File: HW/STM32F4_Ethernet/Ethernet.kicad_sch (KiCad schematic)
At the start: 23 parts, among them J1 LU1T516-43, J2 LU1T516-43, U1 KSZ8863MLLI

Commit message: Progress backup
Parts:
- added C? (x4): 100uF, symbol Device:C_Small
- added C? (x6): 100nF, symbol Device:C_Small
- added C?: 10uF, symbol Device:C
- added D?: 1N4148W, Diode_SMD:D_SOD-123, symbol Diode:1N4148W
- added FB? (x2): MPZ1608S601A, BEADC1608X95N, symbol MPZ1608S601A:MPZ1608S601A
- added FB?: FerriteBead, symbol Device:FerriteBead
- added R? (x3): 10K, symbol Device:R_Small
- added R?: 11.8K, symbol Device:R_Small
- added R? (x2): 4.7K, symbol Device:R_Small
- added R?: 10K, symbol Device:R
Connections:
- net GLED_1 is gone; now on net P1LED0: R1.2
- net GLED_2 is gone; now on net P2LED0: R7.2
- net RLED_1 is gone; now on net P1LED1: R2.2
- net RLED_2 is gone; now on net P2LED1: R8.2
- net +3V3: now also U1.22 (VDDIO), U1.40 (VDDIO_2), C?.1, C?.1, C?.1, D?.1 (K), FB?.1, R?.1, R?.1, R?.1, R?.1
- net GND: now also C?.2, C?.2, C?.2, C?.2, C?.2, C?.2, C?.2, C?.2, C?.2, C?.2, C?.2, FB?.2, R?.2, R?.2, R?.2
- net GNDREF: now also FB?.1
- net RXM1: now also U1.1 (RXM1)
- net RXM2: now also U1.8 (RXM2)
- net RXP1: now also U1.2 (RXP1)
- net RXP2: now also U1.9 (RXP2)
- net TXM1: now also U1.3 (TXM1)
- net TXM2: now also U1.11 (TXM2)
- net TXP1: now also U1.4 (TXP1)
- net TXP2: now also U1.12 (TXP2)
- net CLK_25Mhz: now reaches U1.14 (X1)
- net MII_TX_EN: now reaches U1.16 (SMTXEN3)
- net MII_TXD3: now reaches U1.17 (SMTXD33/E_REFCLK_3)
- net MII_TXD2: now reaches U1.18 (SMTXD32)
- net MII_TXD1: now reaches U1.19 (SMTDX31)
- net MII_TXD0: now reaches U1.20 (SMTXD30)
- net MII_TX_CLK: now reaches U1.23 (SMTXC3/REFCLK_3)
- net MII_LINK_MODE: now reaches U1.24 (SMTXER3/MII_LINK_3)
- net MII_LINK_MODE: now also R?.1
- net MII_RX_DV: now reaches U1.25 (SMRXDV3)
- net MII_RXD3: now reaches U1.26 (SMRXD33/REFCLKO_3)
- net MII_RXD2: now reaches U1.27 (SMRXD32)
- net MII_RXD1: now reaches U1.28 (SMRXD31)
- net MII_RXD0: now reaches U1.29 (SMRXD30)
- net MII_RX_CLK: now reaches U1.30 (SMRXC3)
- net +1V8: now reaches U1.32 (VDDC)
- net +1V8: now also U1.42 (VDDC0), C?.1, C?.1, C?.1, FB?.1
- net MII_COL: now reaches U1.33 (SCOL3)
- net MII_CRS: now reaches U1.34 (SCRS3)
- net ~{MII_INTRN}: now reaches U1.35 (INTRN)
- net PHY_SPI_CLK: now reaches U1.36 (SCL_MDC)
- net PHY_SPI_MOSI: now reaches U1.37 (SDA_MDIO)
- net PHY_SPI_MISO: now reaches U1.38 (SPIQ)
- net PHY_SPI_CS: now reaches U1.39 (SPISN)
- net P1LED1: now reaches U1.43 (P1LED1)
- net P1LED1: now also R?.2
- net P1LED0: now reaches U1.44 (P1LED0)
- net P1LED0: now also R?.2
- net P2LED1: now reaches U1.45 (P2LED1)
- net P2LED1: now also R?.2
- net P2LED0: now reaches U1.46 (P2LED0)
- net P2LED0: now also R?.1
- net ~{PHY_RESET}: now reaches U1.47 (RSTN)
- net ~{PHY_RESET}: now also C?.1, D?.2 (A), R?.2
- net PHY_3V3A: now reaches U1.5 (VDDA_3.3)
- net PHY_3V3A: now also C?.1, C?.1, FB?.2
- net ISET: now reaches U1.6 (ISET)
- net ISET: now also R?.1
- net ETH_1V8 renamed PHY_1V8A
- net PHY_1V8A: now also C?.1, C?.1, FB?.2
- no-connect marks 6 -> 8
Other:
- note added: "1V8 Pin(32,42)"
- note added: "1V8A Pin(7)"
- note added: "2kV / 1000pF Cap. Included"
- note added: "3V3 Pin(22, 40)"
- note added: "3V3A Pin(5)"
- note added: "LED0 : Green - Link LED1 : Yellow - Speed"
- note added: "MII_TX_CLK: Place L3 Inner Layer"
- note added: "Output Transmit Current w/ 11.8K 1%"
- note added: "P1LED0 Strap option: Enable auto-negotiation on port 1 (P1ANEN) PU = Enable (better to pull up in design) PD = Disable (default)"
- note added: "P1LED1 Strap option: Force the speed on port 1 (P1SPD) PU = Force port 1 to 100BT if P1ANEN = 0 PD = Force port 1 to 10BT if P1ANEN = 0"
- note added: "P2LED1, P2LED0 [0, 0] : I2C Master P2LED1, P2LED0 [0, 1] : I2C Slave P2LED1, P2LED0 [1, 0] : SPI Slave P2LED1, P2LED0 [1, 1] : SMI"
- note added: "P2LED1/P2LED0 [0,0] : I2C MASTER [0,1] : I2C SLAVE [1,0] : SPI SLAVE [1,1] : SMI/MIIM"
- moved on the sheet: U1

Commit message: Progress backup. add SRAM
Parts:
- gave numbers to parts that had none: 22
- renumbered C4 to C25, C3 to C26, C1 to C27, C2 to C28, C5 to C29, C6 to C30, D1 to D3, D2 to D4, R8 to R10, R3 to R13, R4 to R14, R5 to R15, R6 to R16, R9 to R17, R10 to R18, R11 to R19, R12 to R20, R1 to R7, R2 to R8, R7 to R9, U1 to U3

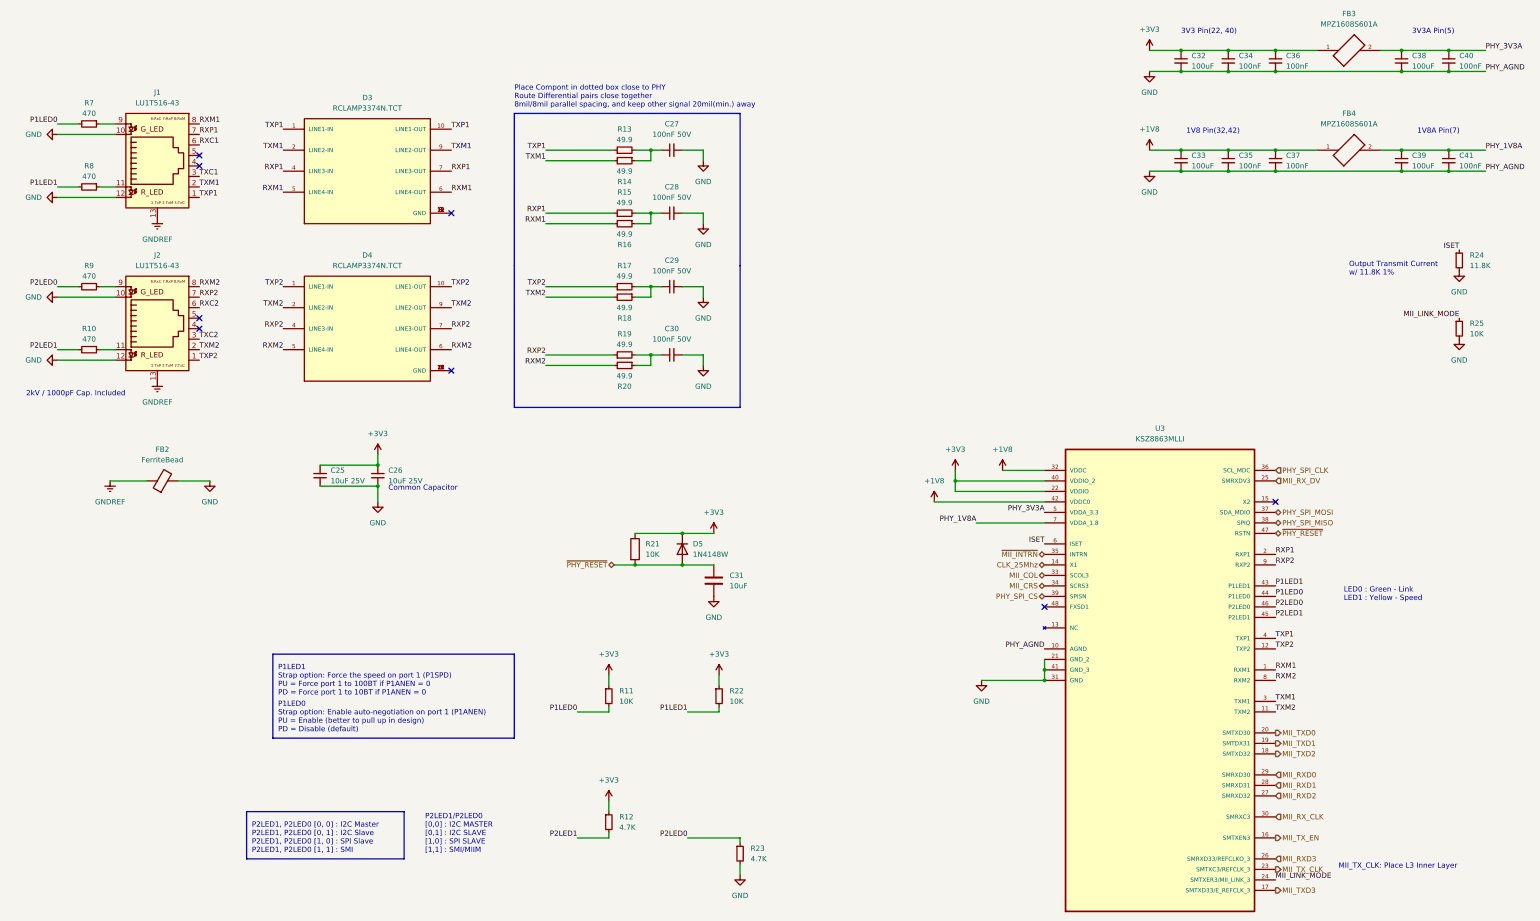
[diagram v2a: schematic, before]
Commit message: Sample PCB. Need to update RLC Size
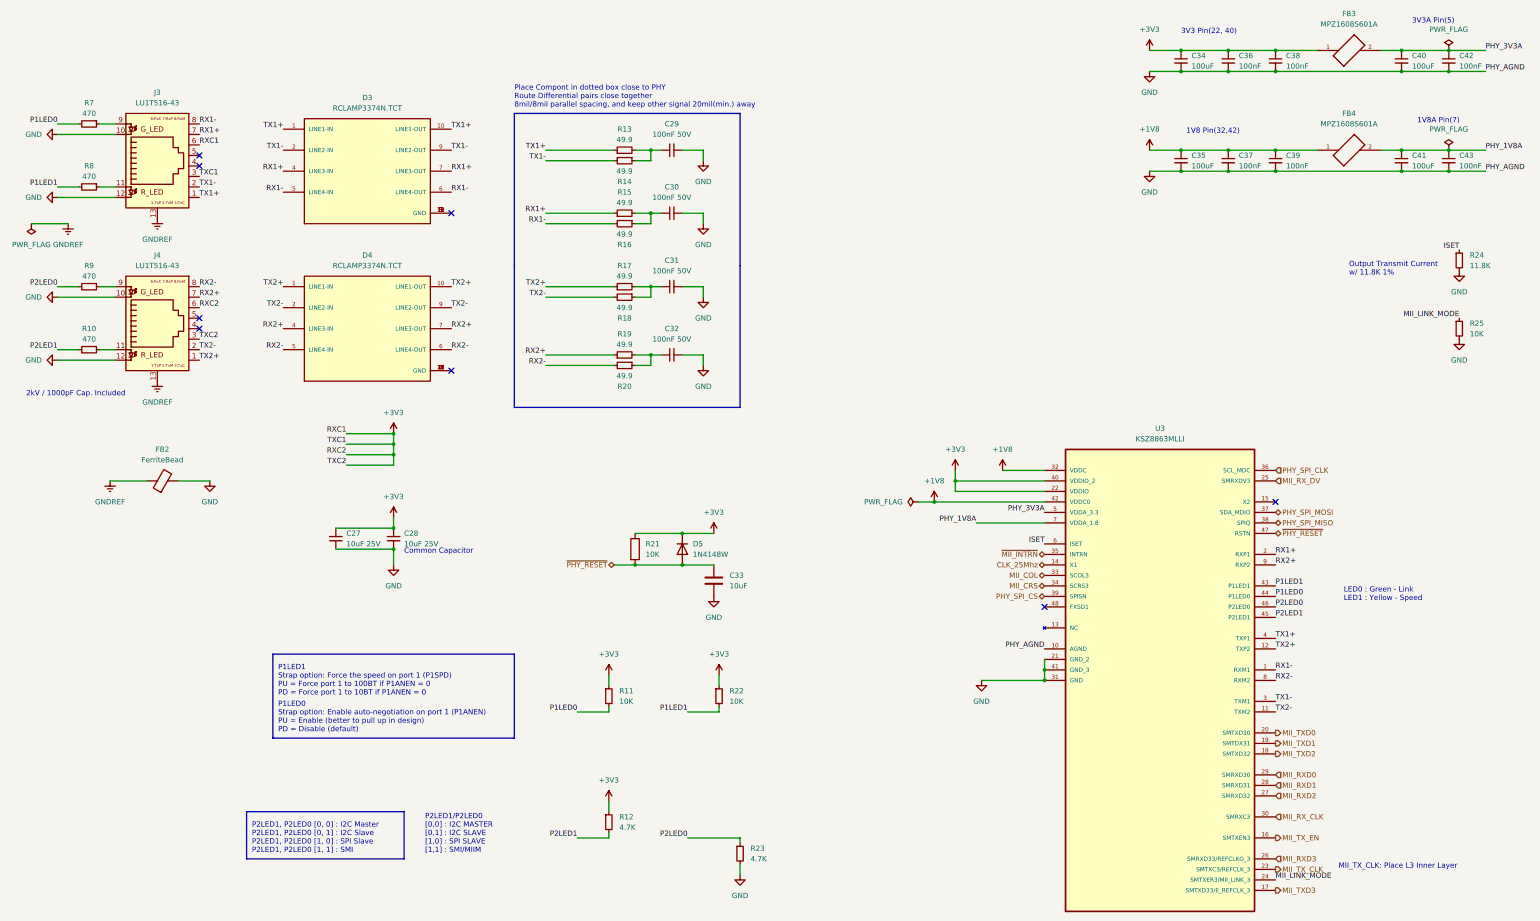
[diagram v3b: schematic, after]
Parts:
- C33: renamed from C31; footprint (none) -> Capacitor_SMD:C_0603_1608Metric_Pad1.08x0.95mm_HandSolder
- C34: renamed from C32; footprint (none) -> Capacitor_SMD:C_0603_1608Metric_Pad1.08x0.95mm_HandSolder
- C35: renamed from C33; footprint (none) -> Capacitor_SMD:C_0603_1608Metric_Pad1.08x0.95mm_HandSolder
- C36: renamed from C34; footprint (none) -> Capacitor_SMD:C_0603_1608Metric_Pad1.08x0.95mm_HandSolder
- C37: renamed from C35; footprint (none) -> Capacitor_SMD:C_0603_1608Metric_Pad1.08x0.95mm_HandSolder
- C38: renamed from C36; footprint (none) -> Capacitor_SMD:C_0603_1608Metric_Pad1.08x0.95mm_HandSolder
- C39: renamed from C37; footprint (none) -> Capacitor_SMD:C_0603_1608Metric_Pad1.08x0.95mm_HandSolder
- C40: renamed from C38; footprint (none) -> Capacitor_SMD:C_0603_1608Metric_Pad1.08x0.95mm_HandSolder
- C41: renamed from C39; footprint (none) -> Capacitor_SMD:C_0603_1608Metric_Pad1.08x0.95mm_HandSolder
- C42: renamed from C40; footprint (none) -> Capacitor_SMD:C_0603_1608Metric_Pad1.08x0.95mm_HandSolder
- C43: renamed from C41; footprint (none) -> Capacitor_SMD:C_0603_1608Metric_Pad1.08x0.95mm_HandSolder
- FB2: footprint (none) -> MPZ1608S601A:BEADC1608X95N
- FB3, FB4: footprint BEADC1608X95N -> MPZ1608S601A:BEADC1608X95N
- R11, R12, R21, R22, R23, R24, R25: footprint (none) -> Resistor_SMD:R_0603_1608Metric_Pad0.98x0.95mm_HandSolder
- renumbered C25 to C27, C26 to C28, C27 to C29, C28 to C30, C29 to C31, C30 to C32, J1 to J3, J2 to J4
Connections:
- net RXC1 is gone; now on net +3V3: J3.6
- net RXC2 is gone; now on net +3V3: J4.6
- net TXC1 is gone; now on net +3V3: J3.3
- net TXC2 is gone; now on net +3V3: J4.3
- net RXM1 renamed RX1-
- net RXM2 renamed RX2-
- net RXP1 renamed RX1+
- net RXP2 renamed RX2+
- net TXM1 renamed TX1-
- net TXM2 renamed TX2-
- net TXP1 renamed TX1+
- net TXP2 renamed TX2+
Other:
- moved on the sheet: C27, C28
